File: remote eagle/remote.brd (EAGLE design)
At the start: 40.4 x 40.4 mm, 17 parts, among them IC1 ATmega328p, J1 ISP Touch, Y1 16MHz, Y2 ANTENNA2ANTENNA-CHIP_1204

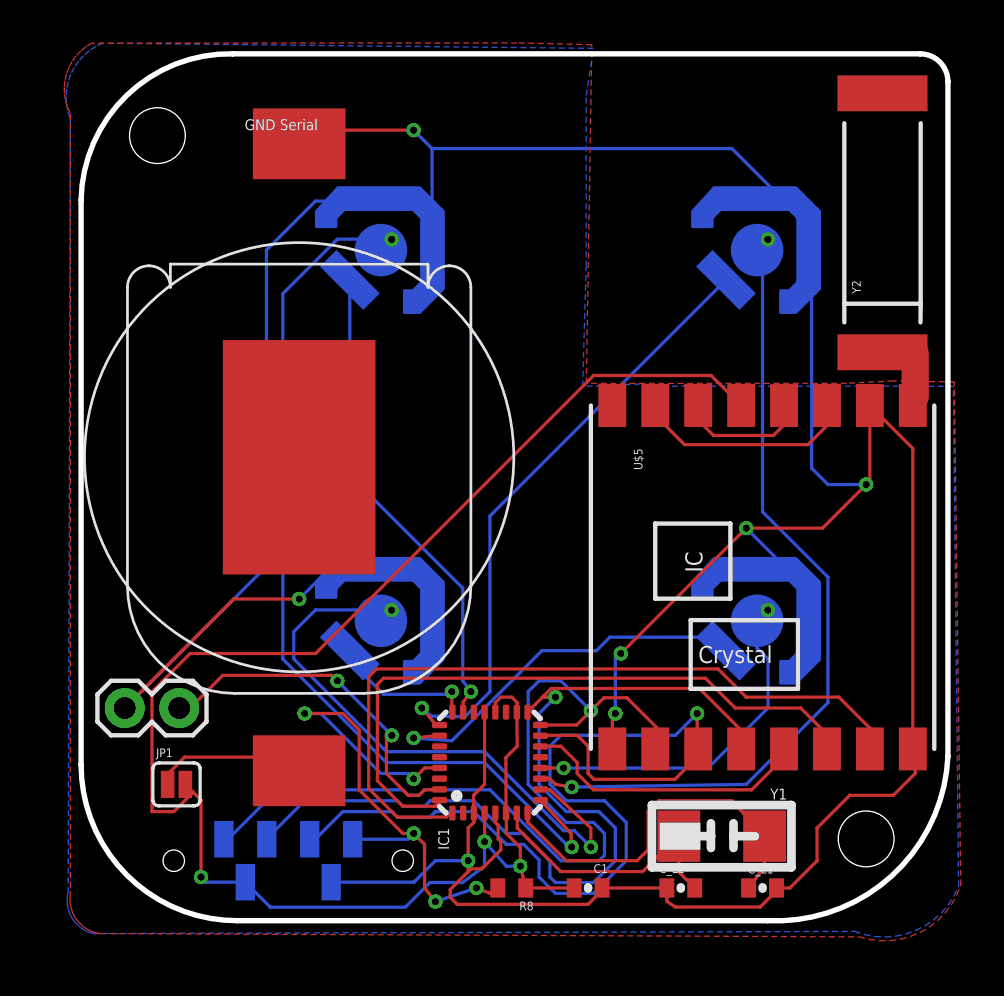
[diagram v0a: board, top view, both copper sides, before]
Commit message: Switching to BLE112 and new P-Series dome by Snaptron in schematic and board.
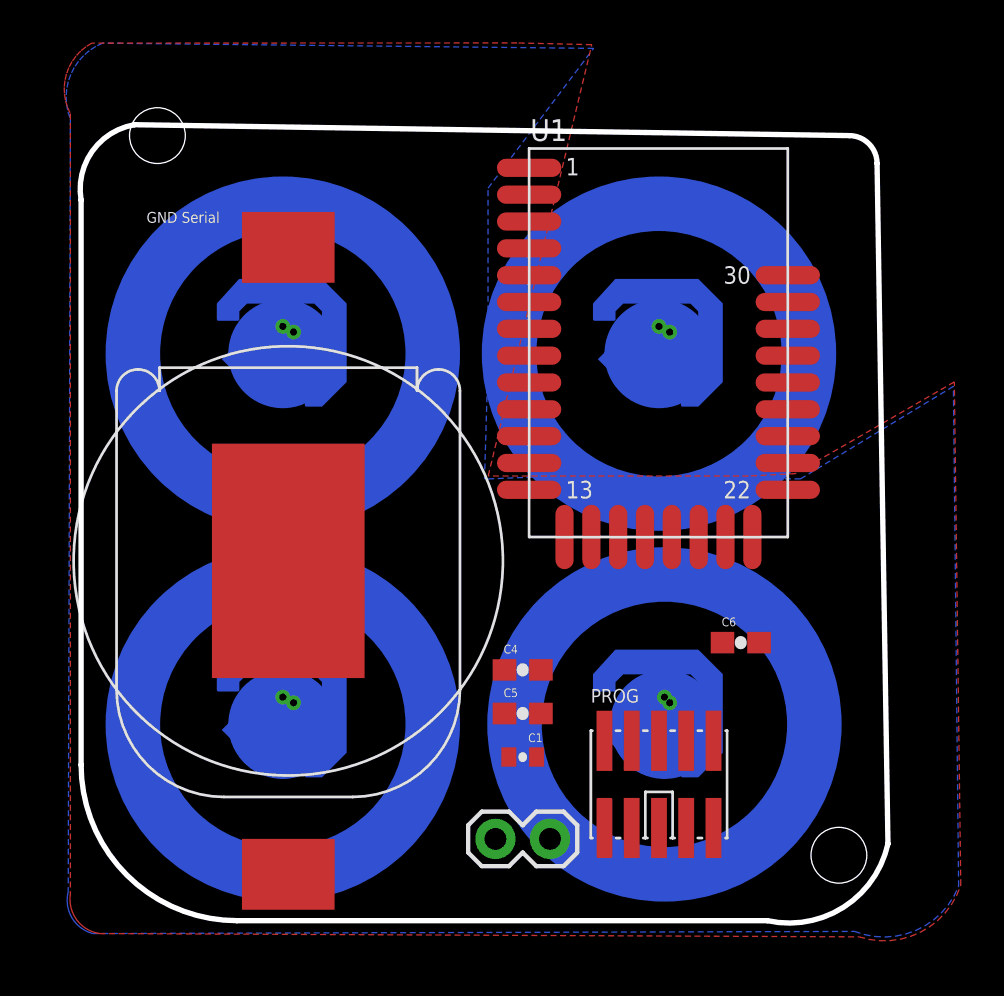
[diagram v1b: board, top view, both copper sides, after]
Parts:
- removed C_L1, C_L2: 8pF, SparkFun-Passives:0402-CAP
- removed IC1: ATmega328p, atmel:MLF32
- removed J1: ISP Touch, remote:AVX_9188_6-WAY_MATING_GUIDE
- removed JP1: (no value), SparkFun-Passives:SJ_2S
- removed R8: 10k, resistor:R0402
- removed U$5: RFM22SMD, remote:RFM22-XXX-S2
- removed Y1: 16MHz, remote:NX5032GA
- removed Y2: ANTENNA2ANTENNA-CHIP_1204, remote:ANTENNA-CHIP_1204
- added C4, C5, C6: 1uF, SparkFun:0603-CAP
- added PROG: CONN_5-2-FTSH-V, pel_misc:FTSH-105-DV
- added U$1, U$2, U$3, U$4: SNAPTRON-DOME, remote:DOME-M-SERIES
- added U1: BLE112-A, sf-bluegiga:BLE112-A
- moved JP2 18.3 mm to (19.3, 3.81)
- moved C1 6.82 mm to (20.6, 7.62)
- moved U$7 6.29 mm to (9.40, 26.9)
- moved U$8 6.29 mm to (9.40, 9.65)
- moved U$10 6.29 mm to (26.9, 9.65)
- moved U$9 6.29 mm to (26.9, 26.9)
- moved LOGO 6.29 mm to (3.05, 22.6)
- moved U$6 4.85 mm to (9.65, 16.8)
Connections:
- removed net CE: IC1.32, U$5.14
- removed net CSN: IC1.14, U$5.13
- removed net MISO: IC1.16, J1.1, U$5.10
- removed net MOSI: IC1.15, J1.4, U$5.11
- removed net N$2: U$5.1, Y2.FEED
- removed net N$3: U$5.3, U$5.7
- removed net N$4: U$5.4, U$5.6
- removed net SCK: IC1.17, J1.3, U$5.12
- removed net SHUTDOWN: IC1.1, U$5.15
- removed net VMM: JP1.1, U$6.P$1
- removed net XTL1: C_L2.2, IC1.7, Y1.P$2
- removed net XTL2: C_L1.2, IC1.8, Y1.P$1
- new net 3.3V: C4.1, C5.1, C6.2, PROG.2, PROG.9, U1.AVDD1, U1.AVDD2, U1.DVDD, U1.VDD_USB
- new net P0_0: U1.P0_0
- new net P0_1: U1.P0_1
- new net P0_2: U1.P0_2
- new net P0_3: U1.P0_3
- new net P0_4: U1.P0_4
- new net P0_5: U1.P0_5
- new net P0_6: U1.P0_6
- new net P0_7: U1.P0_7
- new net P1_0: U1.P1_0
- new net P1_1: U1.P1_1
- new net P1_2: U1.P1_2
- new net P1_3: U1.P1_3
- new net P1_4: U1.P1_4
- new net P1_5: U1.P1_5
- new net P1_6: U1.P1_6
- new net P1_7: U1.P1_7
- new net P2_0: U1.P2_0
- new net P2_1: PROG.4, U1.P2_1
- new net P2_2: PROG.3, U1.P2_2
- new net USB+: U1.USB+
- new net USB-: U1.USB-
- net BUTTON1: no longer IC1.9
- net BUTTON2: no longer IC1.10
- net BUTTON3: no longer IC1.11
- net BUTTON4: no longer IC1.12
- net GND: now also C4.2, C5.2, C6.1, PROG.1, U1.GND1, U1.GND2, U1.GND3, U1.GND4; no longer C_L1.1, C_L2.1, IC1.21, IC1.3, IC1.5, J1.6, U$5.16, U$5.2, U$5.9
- net RESET: now also PROG.7, U1.RESET; no longer IC1.29, J1.5, R8.2
- net SERIAL: no longer IC1.31
- net TOUCH1: no longer IC1.23
- net TOUCH2: no longer IC1.24
- net TOUCH3: no longer IC1.25
- net TOUCH4: no longer IC1.26
- net VCC: now also U$6.P$1; no longer IC1.18, IC1.20, IC1.4, IC1.6, J1.2, JP1.2, R8.1, U$5.5
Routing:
- net GND: track 190.3 -> 0.00 mm, vias 7 -> 0
- net VCC: track 78.9 -> 0.00 mm, vias 3 -> 0
- net MOSI: track 44.9 -> 0.00 mm, vias 1 -> 0
- net BUTTON1: track 44.1 -> 0.00 mm, vias 1 -> 0
- net SCK: track 42.6 -> 0.00 mm, vias 1 -> 0
- net MISO: track 41.9 -> 0.00 mm, vias 1 -> 0
- net BUTTON3: track 38.3 -> 0.00 mm, vias 1 -> 0
- net SHUTDOWN: track 35.5 -> 0.00 mm
- net CE: track 31.0 -> 0.00 mm
- net TOUCH3: track 28.7 -> 0.00 mm, vias 1 -> 0
- net BUTTON2: track 28.1 -> 0.00 mm, vias 1 -> 0
- net RESET: track 26.5 -> 0.00 mm, vias 5 -> 0
- net TOUCH1: track 22.6 -> 0.00 mm, vias 1 -> 0
- net TOUCH4: track 18.1 -> 0.00 mm, vias 1 -> 0
- net XTL2: track 17.8 -> 0.00 mm
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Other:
- board size 40.4 x 40.4 mm -> 37.6 x 37.2 mm

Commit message: New P-Series Dome by Snaptron in the eagle pcb. Layout done for revision 14.
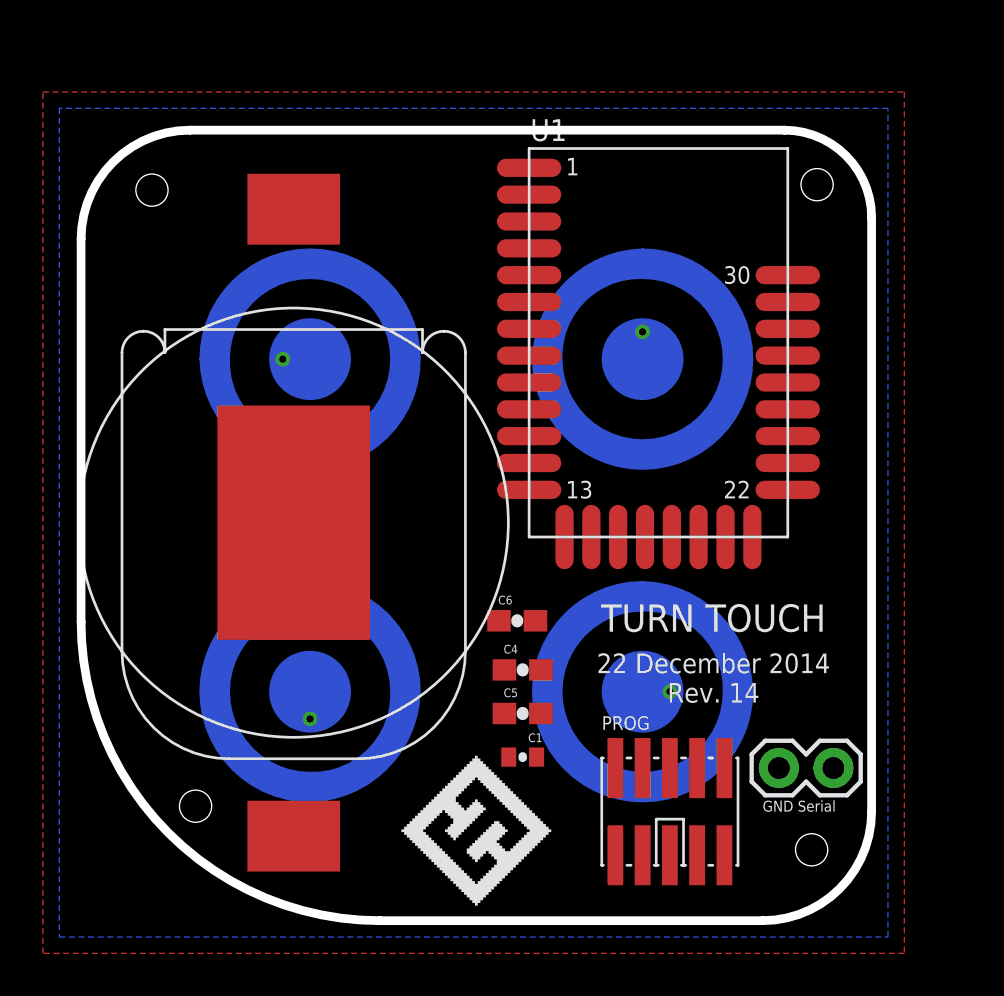
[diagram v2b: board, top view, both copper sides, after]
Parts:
- removed U$10: Button 4, remote:SWITCH-SPDT-SMD
- removed U$7: Button 1, remote:SWITCH-SPDT-SMD
- removed U$8: Button 2, remote:SWITCH-SPDT-SMD
- removed U$9: Button 3, remote:SWITCH-SPDT-SMD
- moved LOGO 24.9 mm to (15.0, 0.76), flipped to the top
- moved U$3 17.1 mm to (10.7, 26.2), turned to 270 degrees
- moved U$1 16.8 mm to (26.2, 26.2)
- moved U$4 16.6 mm to (10.7, 10.7), turned to 180 degrees
- moved U$2 15.8 mm to (26.2, 10.7), turned to 90 degrees
- moved JP2 13.6 mm to (32.5, 7.11)
- moved C6 10.5 mm to (20.3, 14.0)
- moved U$6 1.80 mm to (9.91, 18.5)
- moved PROG 1.37 mm to (27.4, 5.08)
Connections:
- removed net P0_0: U1.P0_0
- removed net P0_1: U1.P0_1
- removed net P0_2: U1.P0_2
- removed net P0_3: U1.P0_3
- removed net P1_0: U1.P1_0
- removed net P1_1: U1.P1_1
- removed net P1_2: U1.P1_2
- removed net P1_3: U1.P1_3
- removed net P1_4: U1.P1_4
- removed net TOUCH1: U$7.TCH
- removed net TOUCH2: U$8.TCH
- removed net TOUCH3: U$9.TCH
- removed net TOUCH4: U$10.TCH
- removed net VCC: C1.1, U$6.P$1
- net 3.3V: now also C1.1, U$1.P.C$1@1, U$1.P.C$1@2, U$2.P.C$1@1, U$2.P.C$1@2, U$3.P.C$1@1, U$3.P.C$1@2, U$4.P.C$1@1, U$4.P.C$1@2, U$6.P$1
- net BUTTON1: now also U$1.P.O$1, U1.P0_0, U1.P1_0; no longer U$7.BTN, U$7.BTNVIA
- net BUTTON2: now also U$2.P.O$1, U1.P0_1, U1.P1_1; no longer U$8.BTN, U$8.BTNVIA
- net BUTTON3: now also U$3.P.O$1, U1.P0_2, U1.P1_2; no longer U$9.BTN, U$9.BTNVIA
- net BUTTON4: now also U$4.P.O$1, U1.P0_3, U1.P1_3; no longer U$10.BTN, U$10.BTNVIA
- net GND: no longer U$10.GND, U$7.GND, U$8.GND, U$9.GND
- net SERIAL: now also U1.P1_4
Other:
- board size 37.6 x 37.2 mm -> 36.8 x 36.8 mm
- board text added: "22 December 2014 Rev. 14"
- board text removed: "7 November 2014 Rev. 13"

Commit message: Revision 14 of the board.
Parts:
- removed C1: .1uF, SparkFun-Passives:0402-CAP
- moved C5 24.4 mm to (16.8, 33.8), turned to 180 degrees
- moved C4 20.4 mm to (16.8, 31.8), turned to 180 degrees
- moved C6 8.87 mm to (22.4, 5.33), turned to 90 degrees
- moved LOGO 1.52 mm to (13.5, 0.76)
- moved U1 0.51 mm to (26.4, 26.9)
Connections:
- removed net 3.3V: C1.1, C4.1, C5.1, C6.2, PROG.2, PROG.9, U$1.P.C$1@1, U$1.P.C$1@2, U$2.P.C$1@1, U$2.P.C$1@2, U$3.P.C$1@1, U$3.P.C$1@2, U$4.P.C$1@1, U$4.P.C$1@2, U$6.P$1, U1.AVDD1, U1.AVDD2, U1.DVDD, U1.VDD_USB
- new net VCC: C4.1, C5.1, C6.2, PROG.2, PROG.9, U$1.P$1, U$1.P$2, U$2.P$1, U$2.P$2, U$3.P$1, U$3.P$2, U$4.P$1, U$4.P$2, U$6.P$1, U1.AVDD1, U1.AVDD2, U1.DVDD, U1.VDD_USB
- net BUTTON1: now also U$1.P$3; no longer U$1.P.O$1
- net BUTTON2: now also U$2.P$3; no longer U$2.P.O$1
- net BUTTON3: now also U$3.P$3; no longer U$3.P.O$1
- net BUTTON4: now also U$4.P$3; no longer U$4.P.O$1
- net GND: no longer C1.2
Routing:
- net VCC: track 0.00 -> 123.1 mm
- net GND: track 0.00 -> 103.3 mm, vias 0 -> 7
- net SERIAL: track 0.00 -> 88.2 mm, vias 0 -> 2
- net BUTTON4: track 0.00 -> 68.9 mm, vias 0 -> 2
- net BUTTON3: track 0.00 -> 50.2 mm, vias 0 -> 2
- net BUTTON2: track 0.00 -> 41.5 mm, vias 0 -> 2
- net P2_2: track 0.00 -> 40.3 mm
- net P2_1: track 0.00 -> 35.8 mm
- net RESET: track 0.00 -> 33.6 mm
- net BUTTON1: track 0.00 -> 28.7 mm, vias 0 -> 2
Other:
- board text added: "24 December 2014 Rev. 14"
- board text removed: "22 December 2014 Rev. 14"

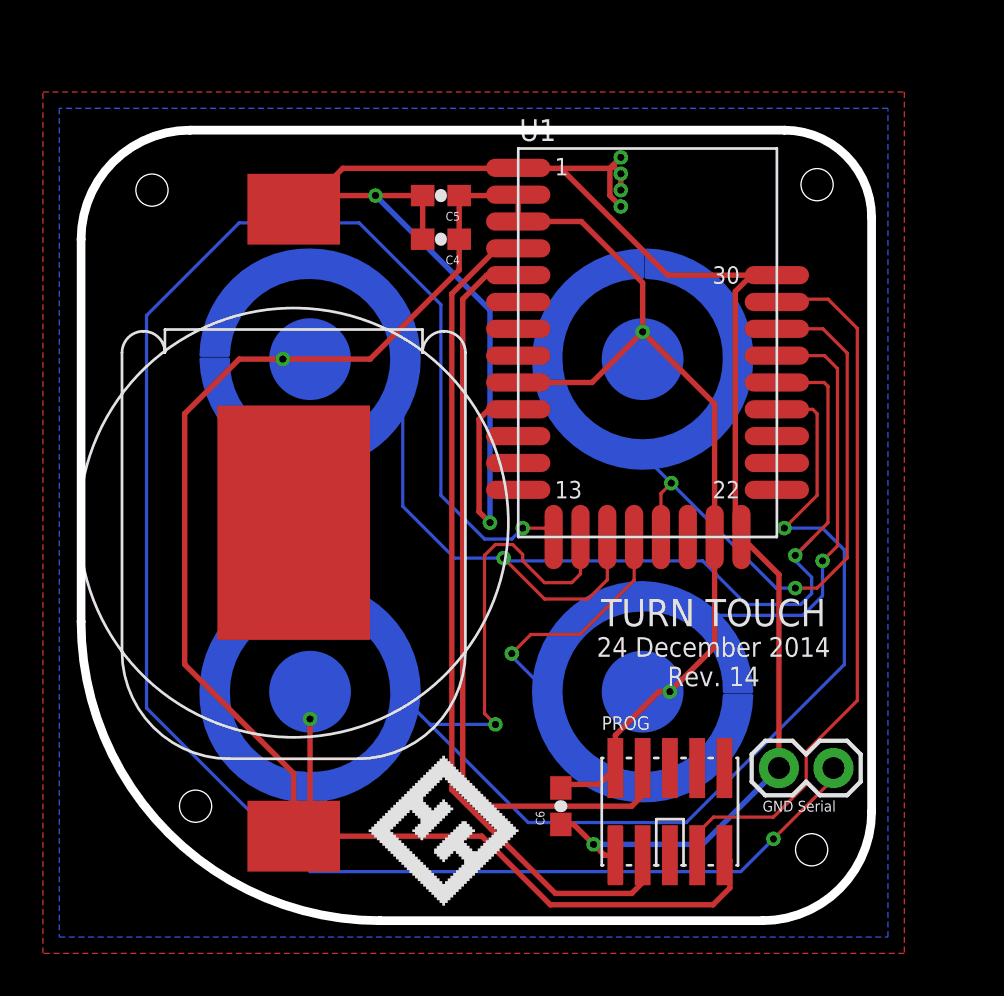
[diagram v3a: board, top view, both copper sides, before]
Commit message: New enclsoure with rev15. Still needs to fix bottom of case supports. Also needs to be split into top and bottom.
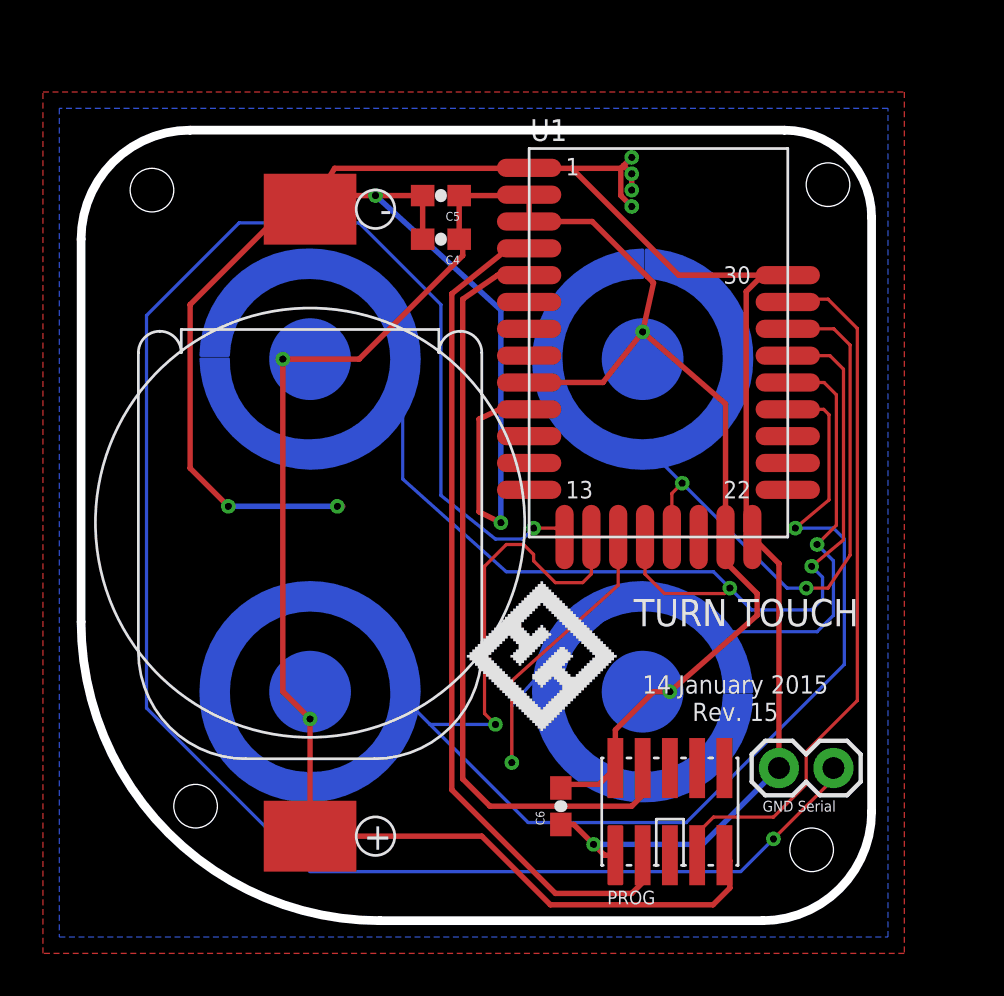
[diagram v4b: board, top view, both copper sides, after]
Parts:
- moved U$2 21.9 mm to (10.7, 26.2), turned to 270 degrees
- moved U$3 21.9 mm to (26.2, 10.7), turned to 90 degrees
- moved LOGO 9.33 mm to (18.0, 8.89)
- moved U$6 0.76 mm to (10.7, 18.5)
- moved U1 0.51 mm to (26.9, 26.9)
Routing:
- net GND: track 103.3 -> 127.4 mm, vias 7 -> 9
- net VCC: track 123.1 -> 114.1 mm
- net BUTTON2: track 41.5 -> 48.4 mm
- net BUTTON3: track 50.2 -> 47.9 mm
- net RESET: track 33.6 -> 33.1 mm
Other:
- board text added: "14 January 2015 Rev. 15"
- board text removed: "24 December 2014 Rev. 14"

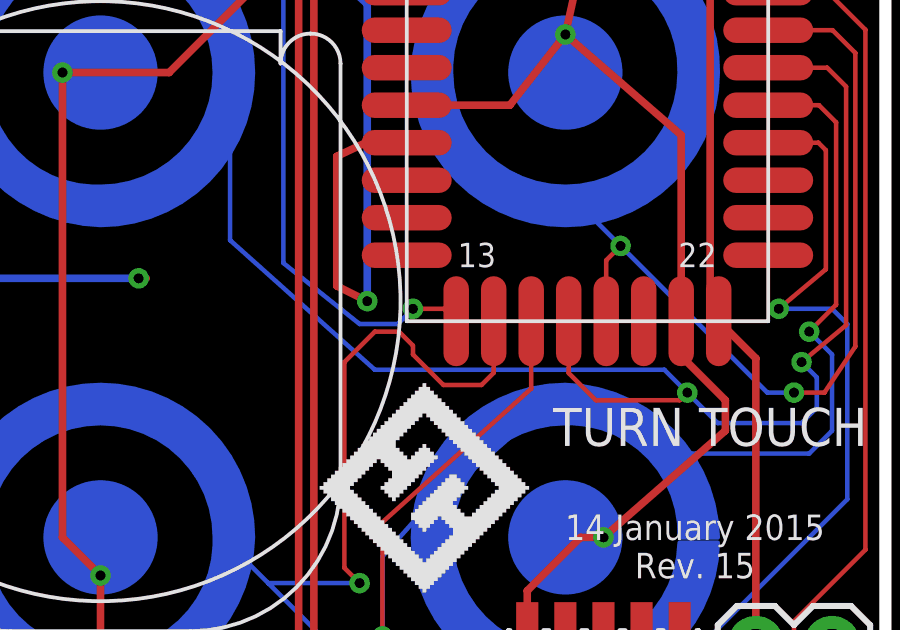
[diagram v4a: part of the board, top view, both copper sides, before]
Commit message: Adding battery level status characteristic and service. Only updates when battery level goes down (except it's in debug mode right now, so it constantly fires).
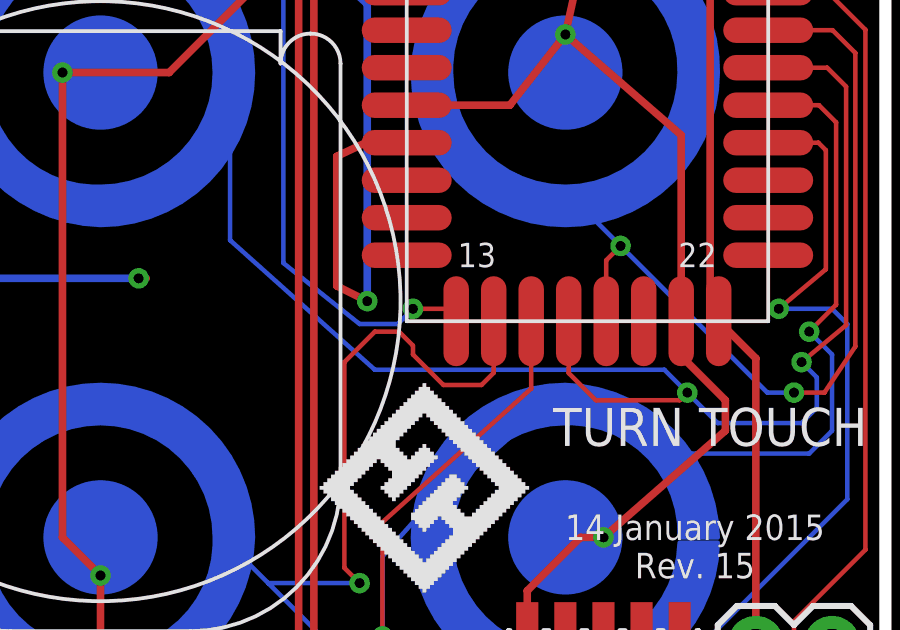
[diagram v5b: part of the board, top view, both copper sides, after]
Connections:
- removed net P0_4: U1.P0_4
- new net P1_4: U1.P1_4
- net SERIAL: now also U1.P0_4; no longer U1.P1_4
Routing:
- net SERIAL: track 88.6 -> 88.0 mm
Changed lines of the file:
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@@
 <signal name="SERIAL">
 <contactref element="JP2" pad="2"/>
-<contactref element="U1" pad="P1_4"/>
 <wire x1="35.052" y1="7.112" x2="35.052" y2="6.604" width="0.1524" layer="1"/>
 <wire x1="35.052" y1="6.604" x2="32.258" y2="3.81" width="0.1524" layer="1"/>
@@
 <via x="21.082" y="18.288" extent="1-16" drill="0.3302"/>
 <wire x1="21.082" y1="18.288" x2="22.11" y2="18.288" width="0.1524" layer="1"/>
-<wire x1="22.11" y1="18.288" x2="22.524" y2="17.874" width="0.1524" layer="1"/>
+<contactref element="U1" pad="P0_4"/>
+<wire x1="22.11" y1="18.288" x2="32.924" y2="22.574" width="0" layer="19" extent="1-1"/>
 </signal>
 <signal name="P2_1">
@@
 <contactref element="U1" pad="P2_0"/>
 </signal>
-<signal name="P0_4">
-<contactref element="U1" pad="P0_4"/>
-</signal>
 <signal name="P0_5">
 <contactref element="U1" pad="P0_5"/>
@@
 <wire x1="28.0035" y1="20.3835" x2="27.1145" y2="21.2725" width="0.1524" layer="16"/>
 </signal>
+<signal name="P1_4">
+<contactref element="U1" pad="P1_4"/>
+</signal>
 </signals>

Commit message: Cleaning up comments. Also removing wakeups, unnecessary for interrupts.
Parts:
- C6: value 1uF -> 100uF
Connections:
- net VCC renamed 3.3V
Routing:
- net 3.3V: track 114.1 -> 22.0 mm
- net GND: track 127.4 -> 100.6 mm, vias 9 -> 7
